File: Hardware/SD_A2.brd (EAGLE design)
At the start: 100.2 x 77.7 mm, 24 parts, among them IC1 74LS245N, IC2 LM1117DTX-3.3, IC3 28C64ASO, IC4 XC9572XL

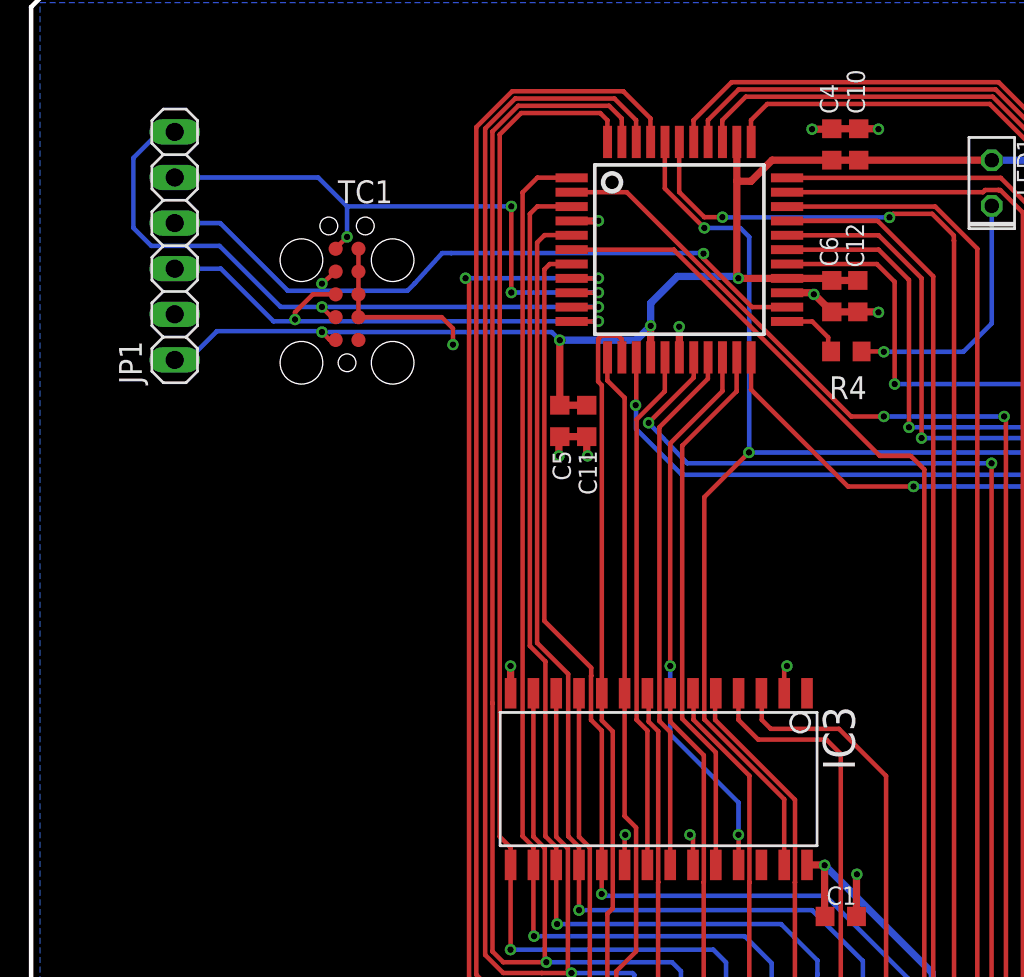
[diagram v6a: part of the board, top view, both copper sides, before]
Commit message: R/W jumper re-added
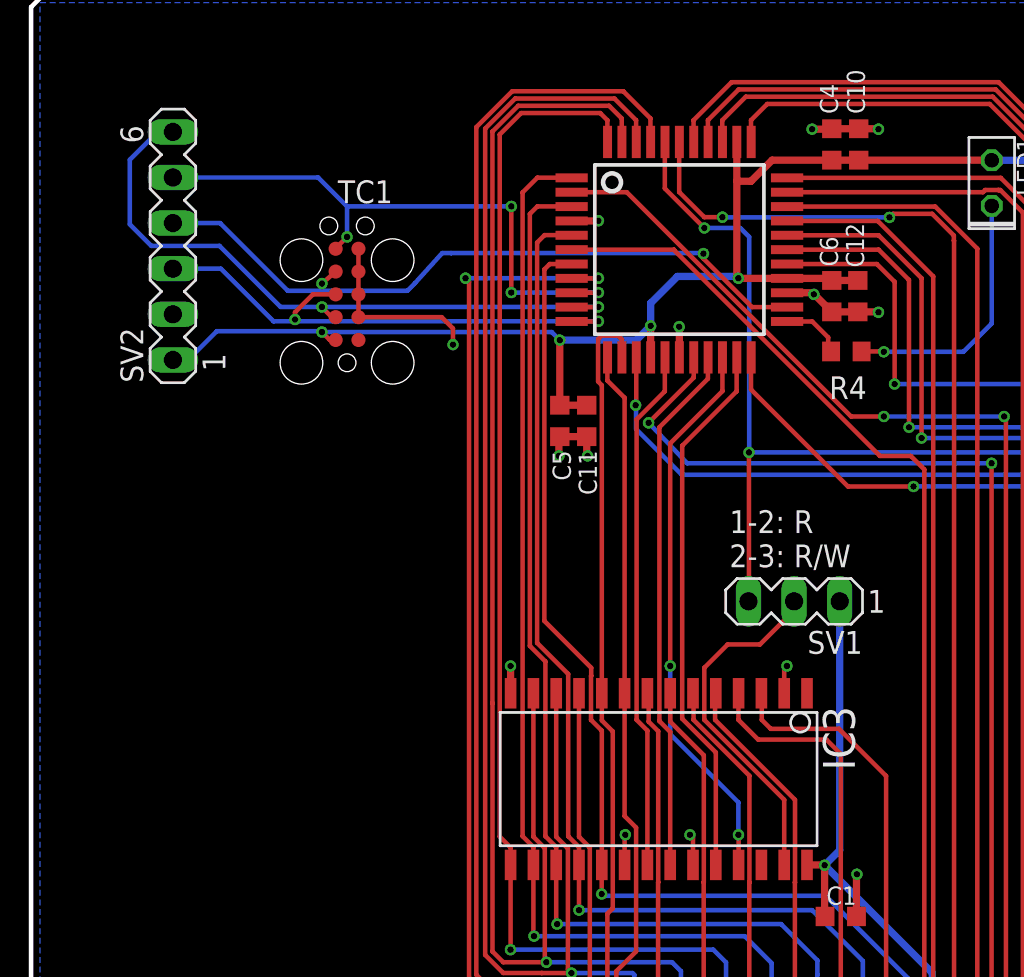
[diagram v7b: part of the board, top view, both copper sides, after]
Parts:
- removed JP1: (no value), pinhead:1X06
- added SV1: (no value), con-lstb:MA03-1
- added SV2: (no value), con-lstb:MA06-1
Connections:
- new net N$1: IC3.27, SV1.2
- net !WE: now also SV1.3; no longer IC3.27
- net +3V3: now also SV2.1; no longer JP1.1
- net +5V: now also SV1.1
- net GND: now also SV2.2; no longer JP1.2
- net TCK: now also SV2.3; no longer JP1.3
- net TDI: now also SV2.5; no longer JP1.5
- net TDO: now also SV2.4; no longer JP1.4
- net TMS: now also SV2.6; no longer JP1.6
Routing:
- net N$1: track 0.00 -> 19.6 mm
- net !WE: track 102.1 -> 84.6 mm
- net +5V: track 76.7 -> 91.7 mm
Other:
- board text added: "1-2: R 2-3: R/W"
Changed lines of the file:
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@@
 <wire x1="100.2" y1="8.4" x2="99.6" y2="7.8" width="0.254" layer="20"/>
 <wire x1="0" y1="8.4" x2="0.6" y2="7.8" width="0.254" layer="20"/>
+<text x="38.9" y="45.8" size="1.27" layer="25" font="vector" ratio="7">1-2: R
+2-3: R/W</text>
 </plain>
 <attributes>
@@
 <attribute name="VALUE" x="95.05" y="23.125" size="1.27" layer="27" rot="R180"/>
 </element>
-<element name="JP1" library="pinhead" package="1X06" value="" x="8" y="63.7" rot="R90"/>
 <element name="TC1" library="TagConnect" package="TC2050-IDC" value="TC2050-IDC" x="17.6" y="61" rot="R90"/>
+<element name="SV1" library="con-lstb" package="MA03-1" value="" x="42.5" y="43.9" rot="R180">
+<attribute name="OC_NEWARK" value="unknown" x="42.5" y="43.9" size="1.778" layer="27" rot="R180" display="off"/>
+<attribute name="MPN" value="" x="42.5" y="43.9" size="1.778" layer="27" rot="R180" display="off"/>
+<attribute name="MF" value="" x="42.5" y="43.9" size="1.778" layer="27" rot="R180" display="off"/>
+<attribute name="OC_FARNELL" value="unknown" x="42.5" y="43.9" size="1.778" layer="27" rot="R180" display="off"/>
+</element>
+<element name="SV2" library="con-lstb" package="MA06-1" value="" x="7.9" y="63.7" rot="R90">
+<attribute name="OC_NEWARK" value="unknown" x="7.9" y="63.7" size="1.778" layer="27" rot="R90" display="off"/>
+<attribute name="MPN" value="" x="7.9" y="63.7" size="1.778" layer="27" rot="R90" display="off"/>
+<attribute name="MF" value="" x="7.9" y="63.7" size="1.778" layer="27" rot="R90" display="off"/>
+<attribute name="OC_FARNELL" value="unknown" x="7.9" y="63.7" size="1.778" layer="27" rot="R90" display="off"/>
+</element>
 </elements>
 <signals>
@@
 <via x="94.5" y="17.1" extent="1-16" drill="0.35"/>
 <wire x1="94.5" y1="18.4" x2="94.5" y2="17.1" width="0.8128" layer="1"/>
-<contactref element="JP1" pad="2"/>
 <contactref element="TC1" pad="9"/>
 <contactref element="TC1" pad="7"/>
@@
 <wire x1="18.235" y1="61" x2="18.235" y2="59.73" width="0.254" layer="1"/>
 <wire x1="18.235" y1="63.54" x2="18.235" y2="62.27" width="0.254" layer="1"/>
+<contactref element="SV2" pad="2"/>
 </signal>
 <signal name="+5V">
@@
 <via x="58.387" y="14" extent="1-16" drill="0.35"/>
 <wire x1="58.387" y1="14" x2="88.248040625" y2="14" width="0.4064" layer="1"/>
+<contactref element="SV1" pad="1"/>
+<wire x1="45.04" y1="43.9" x2="45.04" y2="30.04" width="0.4064" layer="16"/>
+<wire x1="45.04" y1="30.04" x2="44.2" y2="29.2" width="0.4064" layer="16"/>
 </signal>
 <signal name="+3V3">
@@
 <wire x1="94.6" y1="27.7" x2="94.6" y2="32.96" width="0.254" layer="1"/>
 <wire x1="94.6" y1="32.96" x2="94.56" y2="33" width="0.254" layer="1"/>
-<contactref element="JP1" pad="1"/>
 <contactref element="TC1" pad="2"/>
 <wire x1="16.965" y1="58.46" x2="16.74" y2="58.46" width="0.254" layer="1"/>
@@
 <wire x1="10.35" y1="58.95" x2="8.8" y2="57.4" width="0.254" layer="16"/>
 <wire x1="8.8" y1="57.4" x2="8.05" y2="57.4" width="0.254" layer="16"/>
-<wire x1="8.05" y1="57.4" x2="8" y2="57.35" width="0.254" layer="16"/>
+<contactref element="SV2" pad="1"/>
+<wire x1="7.9" y1="57.35" x2="8.05" y2="57.4" width="0" layer="19" extent="16-16"/>
 </signal>
 <signal name="R/!W">
@@
 <wire x1="31.59" y1="59.49" x2="31.6" y2="59.5" width="0.254" layer="1"/>
 <via x="31.6" y="59.5" extent="1-16" drill="0.35"/>
-<contactref element="JP1" pad="3"/>
 <contactref element="TC1" pad="6"/>
 <wire x1="16.965" y1="61" x2="15.7" y2="61" width="0.254" layer="1"/>
 <wire x1="15.7" y1="61" x2="14.7" y2="60" width="0.254" layer="1"/>
-<wire x1="8" y1="62.43" x2="10.57" y2="62.43" width="0.254" layer="16"/>
 <wire x1="10.57" y1="62.43" x2="13.5" y2="59.5" width="0.254" layer="16"/>
 <wire x1="14.7" y1="60" x2="14.7" y2="59.6" width="0.254" layer="1"/>
@@
 <wire x1="14.7" y1="59.5" x2="31.6" y2="59.5" width="0.254" layer="16"/>
 <wire x1="14.7" y1="59.5" x2="14.7" y2="59.6" width="0.254" layer="16"/>
+<contactref element="SV2" pad="3"/>
+<wire x1="10.57" y1="62.43" x2="7.9" y2="62.43" width="0.254" layer="16"/>
 </signal>
 <signal name="TDO">
@@
 <wire x1="40.1526875" y1="60.29" x2="37.452015625" y2="62.990671875" width="0.254" layer="1"/>
 <wire x1="42.11" y1="60.29" x2="40.1526875" y2="60.29" width="0.254" layer="1"/>
-<contactref element="JP1" pad="4"/>
 <contactref element="TC1" pad="8"/>
 <wire x1="37.42215625" y1="63.30055" x2="23.40055" y2="63.30055" width="0.254" layer="16"/>
@@
 <wire x1="16.2" y1="61.2" x2="20.9601125" y2="61.2" width="0.254" layer="16"/>
 <wire x1="16.2" y1="61.6" x2="16.2" y2="61.2" width="0.254" layer="16"/>
-<wire x1="8" y1="64.97" x2="10.53" y2="64.97" width="0.254" layer="16"/>
 <wire x1="10.53" y1="64.97" x2="14.3" y2="61.2" width="0.254" layer="16"/>
+<contactref element="SV2" pad="4"/>
+<wire x1="10.53" y1="64.97" x2="7.9" y2="64.97" width="0.254" layer="16"/>
 </signal>
 <signal name="TDI">
@@
 <wire x1="31.59" y1="61.09" x2="31.6" y2="61.1" width="0.254" layer="1"/>
 <via x="31.6" y="61.1" extent="1-16" drill="0.35"/>
-<contactref element="JP1" pad="5"/>
 <contactref element="TC1" pad="10"/>
 <wire x1="26.75" y1="61.1" x2="31.6" y2="61.1" width="0.254" layer="16"/>
@@
 <wire x1="26.75" y1="65.9" x2="26.75" y2="61.1" width="0.254" layer="1"/>
 <wire x1="17.6" y1="65.9" x2="17.6" y2="64.2" width="0.254" layer="16"/>
-<wire x1="8" y1="67.51" x2="15.99" y2="67.51" width="0.254" layer="16"/>
 <wire x1="15.99" y1="67.51" x2="17.6" y2="65.9" width="0.254" layer="16"/>
+<contactref element="SV2" pad="5"/>
+<wire x1="15.99" y1="67.51" x2="7.9" y2="67.51" width="0.254" layer="16"/>
 </signal>
 <signal name="TMS">
@@
 <wire x1="31.59" y1="60.29" x2="31.6" y2="60.3" width="0.254" layer="1"/>
 <via x="31.6" y="60.3" extent="1-16" drill="0.35"/>
-<contactref element="JP1" pad="6"/>
 <contactref element="TC1" pad="4"/>
 <wire x1="16.965" y1="59.73" x2="16.75" y2="59.73" width="0.254" layer="1"/>
-<wire x1="16.75" y1="59.73" x2="16.29" y2="60.19" width="0.254" layer="1"/>
+<wire x1="16.75" y1="59.73" x2="16.2" y2="60.28" width="0.254" layer="1"/>
 <via x="16.2" y="60.3" extent="1-16" drill="0.35"/>
 <wire x1="16.2" y1="60.28" x2="16.19" y2="60.29" width="0.254" layer="1"/>
@@
 <wire x1="13.9" y1="60.3" x2="10.5" y2="63.7" width="0.254" layer="16"/>
 <wire x1="10.5" y1="63.7" x2="6.7" y2="63.7" width="0.254" layer="16"/>
-<wire x1="6.7" y1="63.7" x2="5.7" y2="64.7" width="0.254" layer="16"/>
-<wire x1="5.7" y1="64.7" x2="5.7" y2="68.6" width="0.254" layer="16"/>
-<wire x1="5.7" y1="68.6" x2="7.2" y2="70.1" width="0.254" layer="16"/>
-<wire x1="7.2" y1="70.1" x2="7.95" y2="70.1" width="0.254" layer="16"/>
-<wire x1="7.95" y1="70.1" x2="8" y2="70.05" width="0.254" layer="16"/>
+<wire x1="7.1" y1="70.1" x2="7.95" y2="70.1" width="0.254" layer="16"/>
 <wire x1="16.2" y1="60.3" x2="31.6" y2="60.3" width="0.254" layer="16"/>
 <wire x1="16.2" y1="60.3" x2="16.2" y2="60.28" width="0.254" layer="1"/>
-<wire x1="16.2" y1="60.28" x2="16.29" y2="60.19" width="0.254" layer="1"/>
+<contactref element="SV2" pad="6"/>
+<wire x1="7.95" y1="70.1" x2="7.9" y2="70.05" width="0.254" layer="16"/>
+<wire x1="7.1" y1="70.1" x2="5.5" y2="68.5" width="0.254" layer="16"/>
+<wire x1="5.5" y1="68.5" x2="5.5" y2="64.9" width="0.254" layer="16"/>
+<wire x1="5.5" y1="64.9" x2="6.7" y2="63.7" width="0.254" layer="16"/>
 </signal>
 <signal name="!IO_STR">
@@
 <signal name="!WE">
 <contactref element="IC4" pad="40"/>
-<contactref element="IC3" pad="27"/>
-<wire x1="41.95" y1="29.22" x2="41.95" y2="32.87865625" width="0.254" layer="1"/>
-<wire x1="41.95" y1="32.87865625" x2="37.5" y2="37.32865625" width="0.254" layer="1"/>
 <wire x1="35.31" y1="69.49" x2="35.31" y2="68.7482625" width="0.254" layer="1"/>
 <via x="37.5" y="64.698" extent="1-16" drill="0.35"/>
@@
 <wire x1="79.3" y1="33.02" x2="79.32" y2="33" width="0.254" layer="1"/>
 <wire x1="39.99903125" y1="52.20738125" x2="39.98565" y2="52.194" width="0.254" layer="16"/>
-<wire x1="37.5" y1="49.70835" x2="39.98565" y2="52.194" width="0.254" layer="1"/>
 <via x="39.98565" y="52.194" extent="1-16" drill="0.35"/>
-<wire x1="37.5" y1="37.32865625" x2="37.5" y2="49.70835" width="0.254" layer="1"/>
 <wire x1="37.5" y1="64.698" x2="39.502" y2="64.698" width="0.254" layer="16"/>
 <wire x1="39.502" y1="64.698" x2="40" y2="64.2" width="0.254" layer="16"/>
 <wire x1="40" y1="64.2" x2="40" y2="52.20835" width="0.254" layer="16"/>
 <wire x1="40" y1="52.20835" x2="39.98565" y2="52.194" width="0.254" layer="16"/>
+<contactref element="SV1" pad="3"/>
+<wire x1="39.98565" y1="52.194" x2="39.98565" y2="43.92565" width="0.254" layer="1"/>
+<wire x1="39.98565" y1="43.92565" x2="39.96" y2="43.9" width="0.254" layer="1"/>
 </signal>
 <signal name="DAT2">
@@
 <wire x1="87" y1="33.06" x2="86.94" y2="33" width="0.254" layer="1"/>
 </signal>
+<signal name="N$1">
+<contactref element="SV1" pad="2"/>
+<contactref element="IC3" pad="27"/>
+<wire x1="41.95" y1="29.22" x2="41.95" y2="32.85" width="0.254" layer="1"/>
+<wire x1="41.95" y1="32.85" x2="37.5" y2="37.3" width="0.254" layer="1"/>
+<wire x1="37.5" y1="37.3" x2="37.5" y2="40.2" width="0.254" layer="1"/>
+<wire x1="42.5" y1="43.9" x2="42.5" y2="43.4" width="0.254" layer="1"/>
+<wire x1="42.5" y1="43.4" x2="40.6" y2="41.5" width="0.254" layer="1"/>
+<wire x1="40.6" y1="41.5" x2="38.8" y2="41.5" width="0.254" layer="1"/>
+<wire x1="38.8" y1="41.5" x2="37.5" y2="40.2" width="0.254" layer="1"/>
+</signal>
 </signals>
